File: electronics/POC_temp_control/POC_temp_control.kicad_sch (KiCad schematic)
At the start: 3 parts, among them J1 Conn_01x02

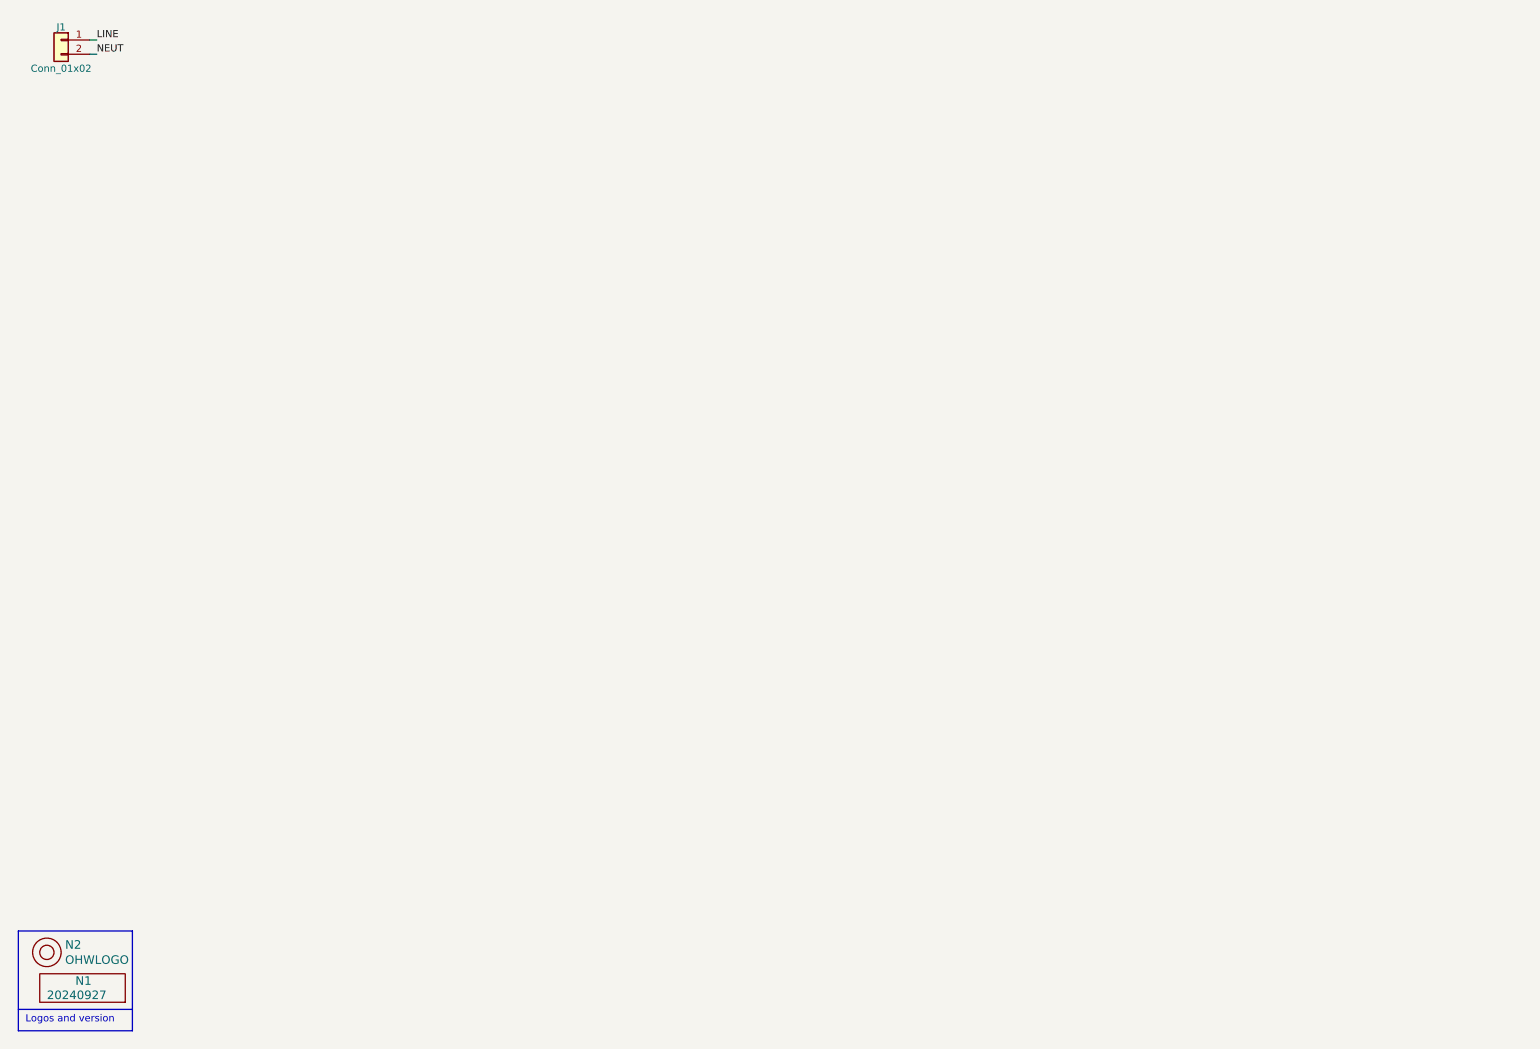
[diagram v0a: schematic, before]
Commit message: added digital supplies and P&R
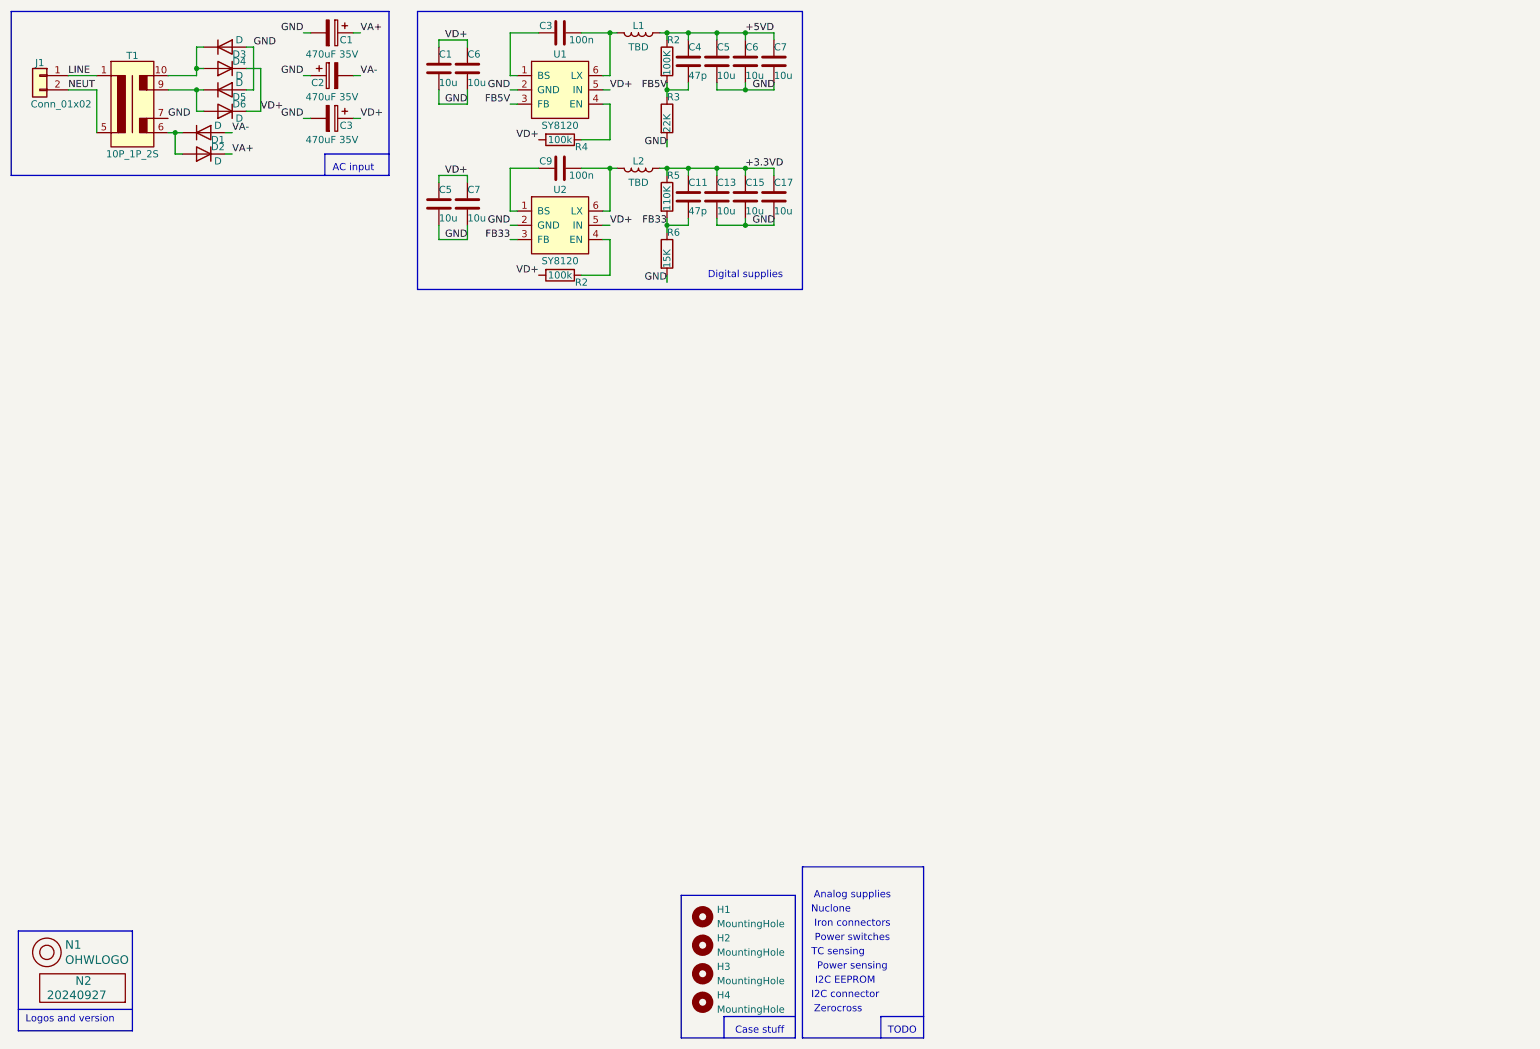
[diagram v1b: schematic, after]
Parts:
- removed N1: 20240927, SquantorLabels:Label_Generic, symbol SquantorLabels:VYYYYMMDD
- added C1, C5, C6, C7: 10u, SquantorCapacitor:C_1206_0805, symbol Device:C
- added C1, C2, C3: 470uF 35V, SquantorCapacitor:C-035-080-elco, symbol Device:C_Polarized
- added C11, C4: 47p, SquantorCapacitor:C_0603, symbol Device:C
- added C13, C15, C17, C5, C6, C7: 10u, SquantorCapacitor:C_0805, symbol Device:C
- added C3, C9: 100n, SquantorCapacitor:C_0603, symbol Device:C
- added D1, D2, D3, D4, D5, D6: D, SquantorDiodes:SOD-123F-hand, symbol Device:D
- added H1, H2, H3, H4: MountingHole, SquantorPcbOutline:MountingHole_3.2mm_M3_Pad_Via, symbol Mechanical:MountingHole
- added L1, L2: TBD, SquantorInductor:L_VLS50XXEX_TDK_hand, symbol Device:L
- added N2: 20240927, SquantorLabels:Label_Generic, symbol SquantorLabels:VYYYYMMDD
- added R2: 100K, SquantorResistor:R_0603_hand, symbol Device:R
- added R2, R4: 100k, SquantorResistor:R_0603_hand, symbol Device:R
- added R3: 22K, SquantorResistor:R_0603_hand, symbol Device:R
- added R5: 110K, SquantorResistor:R_0603_hand, symbol Device:R
- added R6: 15K, SquantorResistor:R_0603_hand, symbol Device:R
- added T1: 10P_1P_2S, SquantorTransformer:10pin_5pitch_32x27_1Pri_2Sec, symbol SquantorTransformer:10P_1P_2S
- added U1, U2: SY8120, SquantorIC:SOT23-6-HAND, symbol SquantorSilergy:SY8120
- renumbered N2 to N1
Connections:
- net LINE: now also T1.1
- net NEUT: now also T1.5
- new net: C3.2, U1.1 (BS)
- new net: R4.1, U1.4 (EN)
- new net: C3.1, L1.2, U1.6 (LX)
- new net: C9.1, L2.2, U2.6 (LX)
- new net: C9.2, U2.1 (BS)
- new net: D3.1 (K), D4.2 (A), T1.10
- new net: D1.1 (K), D2.2 (A), T1.6
- new net: D5.1 (K), D6.2 (A), T1.9
- new net: R2.1, U2.4 (EN)
- new net +3.3VD: C11.1, C13.1, C15.1, C17.1, L2.1, R5.1
- new net +5VD: C4.1, C5.1, C6.1, C7.1, L1.1, R2.1
- new net FB33: C11.2, R5.2, R6.1, U2.3 (FB)
- new net FB5V: C4.2, R2.2, R3.1, U1.3 (FB)
- new net GND: C1.2, C1.2, C13.2, C15.2, C17.2, C2.1, C3.2, C5.2, C5.2, C6.2, C6.2, C7.2, C7.2, D3.2 (A), D5.2 (A), R3.2, R6.2, T1.7, U1.2 (GND), U2.2 (GND)
- new net VA+: C1.1, D2.1 (K)
- new net VA-: C2.2, D1.2 (A)
- new net VD+: C1.1, C3.1, C5.1, C6.1, C7.1, D4.1 (K), D6.1 (K), R2.2, R4.2, U1.5 (IN), U2.5 (IN)
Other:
- note added: "AC input"
- note added: "Analog supplies"
- note added: "Case stuff"
- note added: "Digital supplies"
- note added: "I2C EEPROM"
- note added: "I2C connector"
- note added: "Iron connectors"
- note added: "Nuclone"
- note added: "Power sensing"
- note added: "Power switches"
- note added: "TC sensing"
- note added: "TODO"
- note added: "Zerocross"
- moved on the sheet: J1

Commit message: added analog powersupply
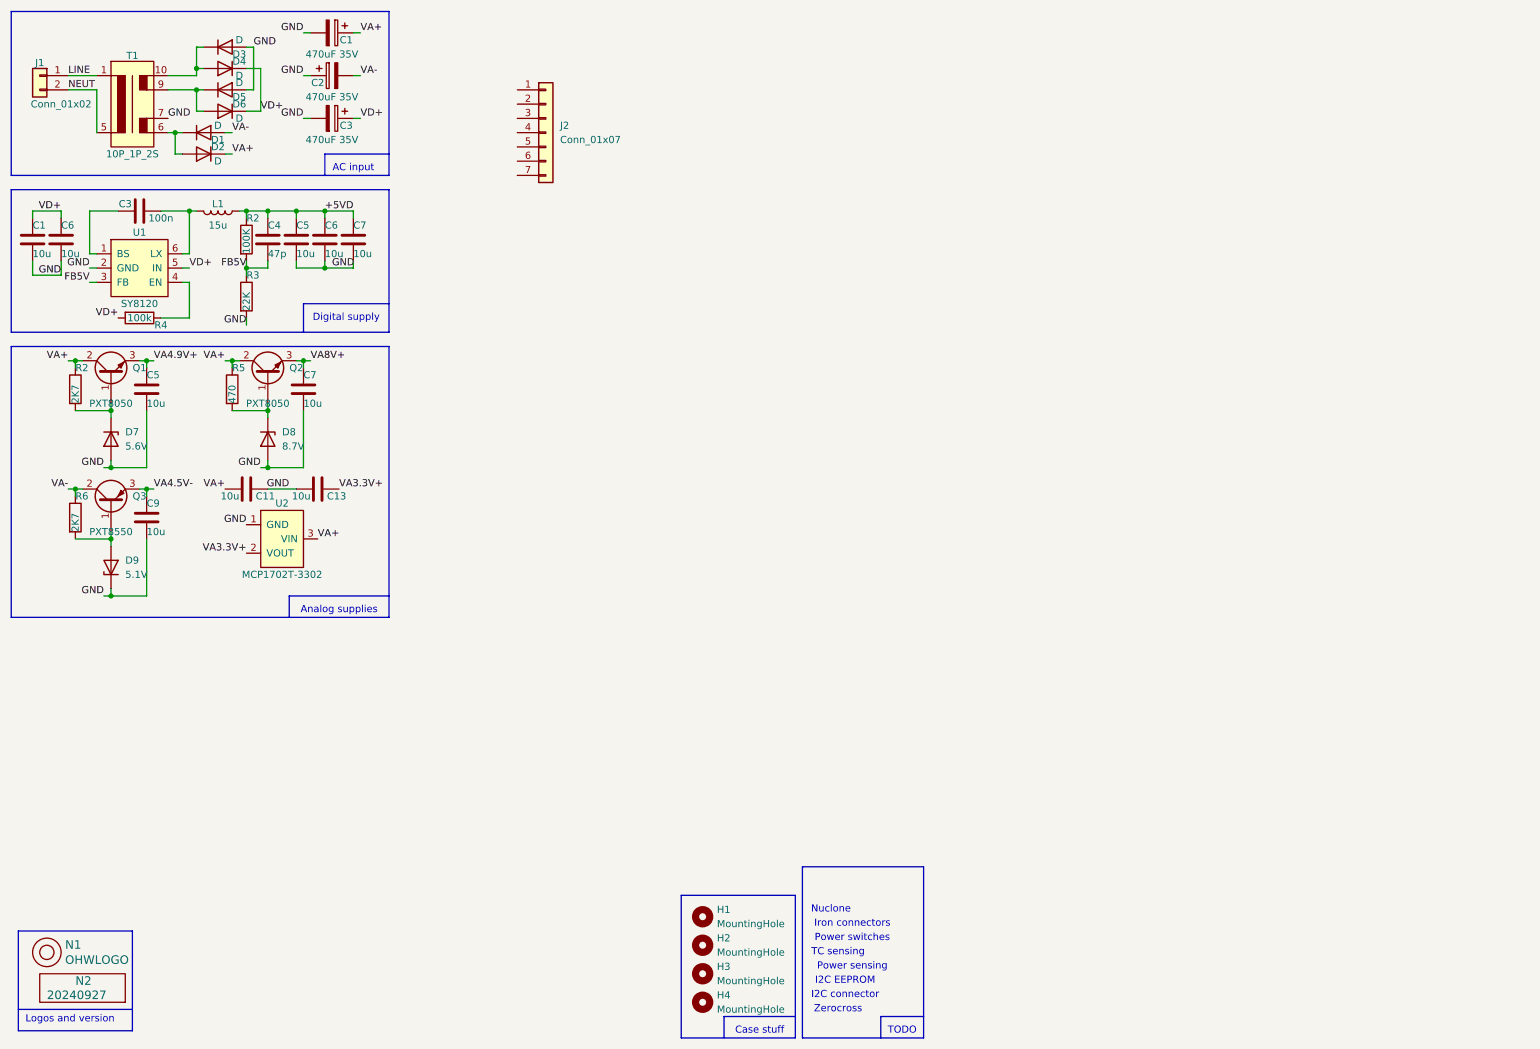
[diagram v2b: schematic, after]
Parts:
- removed C15, C17: 10u, SquantorCapacitor:C_0805, symbol Device:C
- removed L2: TBD, SquantorInductor:L_VLS50XXEX_TDK_hand, symbol Device:L
- removed U2: SY8120, SquantorIC:SOT23-6-HAND, symbol SquantorSilergy:SY8120
- added D7: 5.6V, SquantorDiodes:SOD-123-hand, symbol Device:D_Zener
- added D8: 8.7V, SquantorDiodes:SOD-123-hand, symbol Device:D_Zener
- added D9: 5.1V, SquantorDiodes:SOD-123-hand, symbol Device:D_Zener
- added J2: Conn_01x07, symbol Connector_Generic:Conn_01x07
- added Q1, Q2: PXT8050, SquantorIC:SOT89-NXP, symbol Device:Q_NPN_BCE
- added Q3: PXT8550, SquantorIC:SOT89-NXP, symbol Device:Q_PNP_BCE
- added U2: MCP1702T-3302, SquantorIC:SOT23-3, symbol SquantorGenericAnalog:regulator_sot23
- C11: value 47p -> 10u; footprint SquantorCapacitor:C_0603 -> SquantorCapacitor:C_0805
- C5, C7: footprint SquantorCapacitor:C_1206_0805 -> SquantorCapacitor:C_0805
- C9: value 100n -> 10u; footprint SquantorCapacitor:C_0603 -> SquantorCapacitor:C_0805
- L1: value TBD -> 15u
- R2: value 100k -> 2K7
- R5: value 110K -> 470
- R6: value 15K -> 2K7
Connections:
- net GND: now also C11.2, C13.1, C9.2, D7.2 (A), D8.2 (A), D9.1 (K), U2.1 (GND); no longer C13.2, R6.2
- net VA+: now also C11.1, R2.1, R5.1, Q1.2 (C), Q2.2 (C), U2.3 (VIN)
- net VA-: now also R6.1, Q3.2 (C)
- net VD+: no longer C5.1, C7.1, R2.2
- net VA4.5V-: now reaches C9.1
- net VA4.5V-: now also Q3.3 (E)
- removed net +3.3VD: C11.1, C13.1, R5.1
- removed net FB33: C11.2, R5.2, R6.1
- new net: D7.1 (K), Q1.1 (B), R2.2
- new net: D9.2 (A), Q3.1 (B), R6.2
- new net: D8.1 (K), Q2.1 (B), R5.2
- new net VA3.3V+: C13.2, U2.2 (VOUT)
- new net VA4.9V+: C5.1, Q1.3 (E)
- new net VA8V+: C7.1, Q2.3 (E)
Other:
- note added: "Digital supply"
- note removed: "Digital supplies"
- moved on the sheet: C1, C3, C4, C5, C6, C7, L1, R2, R3, R4, U1

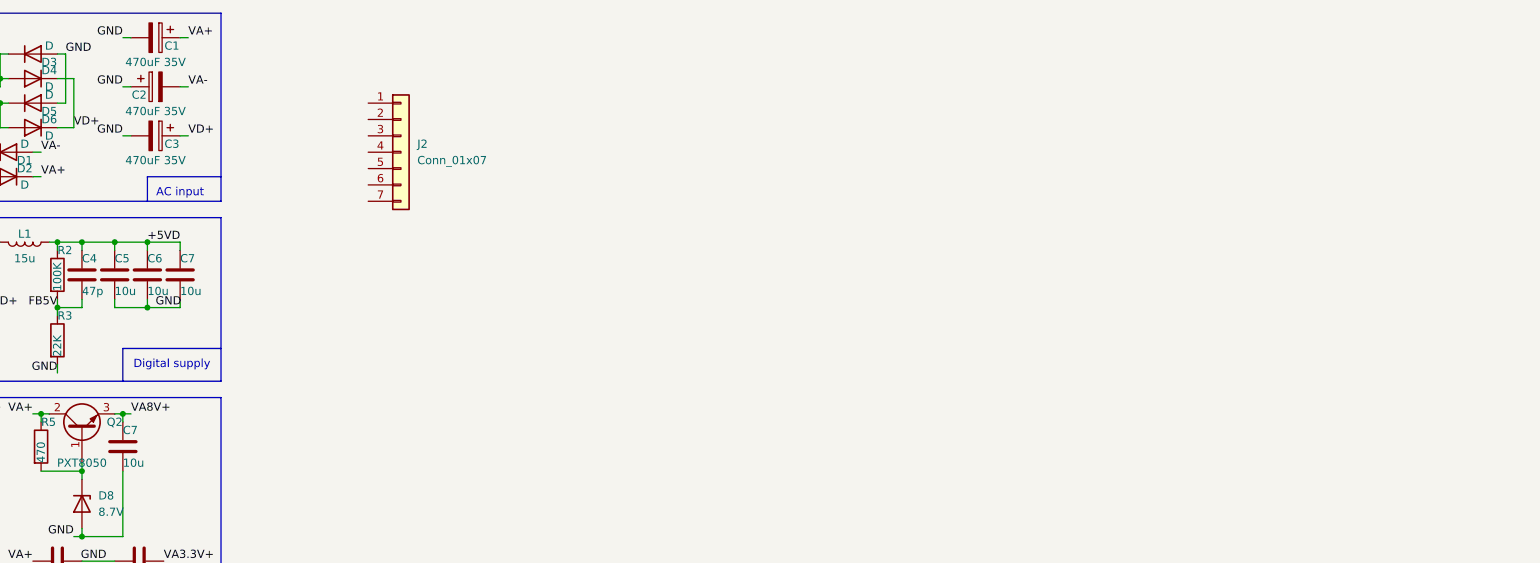
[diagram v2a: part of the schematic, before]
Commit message: added analog supplies, started with nuclone addition
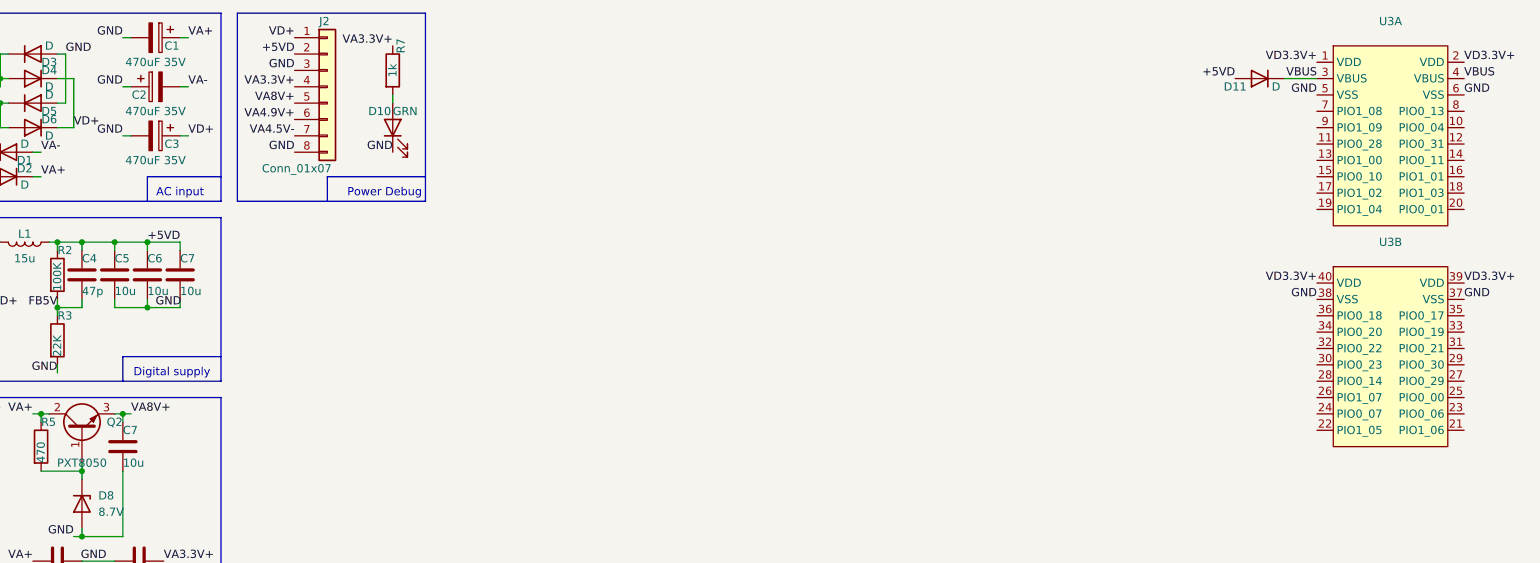
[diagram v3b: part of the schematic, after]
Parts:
- added D10: GRN, SquantorDiodes:LED_0603_hand, symbol Device:LED
- added D11: D, symbol Device:D
- added R7: 1k, SquantorResistor:R_0603_hand, symbol Device:R
- added U3: ~, symbol SquantorNuclone:nuclone_small_LPC845
- J2: footprint (none) -> SquantorConnectors:Header-0254-1X08-H008; symbol Connector_Generic:Conn_01x07 -> Connector_Generic:Conn_01x08
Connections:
- net +5VD: now also J2.2 (Pin_2), D11.2 (A)
- net GND: now also J2.3 (Pin_3), J2.8 (Pin_8), D10.1 (K), U3.37 (VSS), U3.38 (VSS), U3.5 (VSS), U3.6 (VSS)
- net VA3.3V+: now also J2.4 (Pin_4), R7.1
- net VA4.5V-: now also J2.7 (Pin_7)
- net VA4.9V+: now also J2.6 (Pin_6)
- net VA8V+: now also J2.5 (Pin_5)
- net VD+: now also J2.1 (Pin_1)
- new net: D10.2 (A), R7.2
- new net VBUS: D11.1 (K), U3.3 (VBUS), U3.4 (VBUS)
- new net VD3.3V+: U3.1 (VDD), U3.2 (VDD), U3.39 (VDD), U3.40 (VDD)
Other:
- note added: "Power Debug"

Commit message: added nuclone footprint and component
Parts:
- added R10: 10k, SquantorResistor:R_0603_hand, symbol Device:R
- added R9: 5k6, SquantorResistor:R_0603_hand, symbol Device:R
- D11: footprint (none) -> SquantorDiodes:SOD-123F-hand
- U3: footprint (none) -> SquantorNuclone:nuclone_small_LPC845
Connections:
- net +5VD: now also R9.2
- net GND: now also R10.1
- net POWER_SENSE: now reaches U3.10 (PIO0_04)
- net POWER_SENSE: now also R10.2, R9.1
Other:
- moved on the sheet: D11, U3A, U3B
